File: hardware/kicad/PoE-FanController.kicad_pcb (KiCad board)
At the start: 2 copper layers, 70 x 78 mm, 33 parts, among them J2 FAN1, J3 FAN2, J4 FAN3, J5 FAN4, J6 Molex_KK254_3pin, J8 Waveshare_ESP32P4POEETH, U1 LM2587-12

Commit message: hw(#100): rotate J2-J5 fan headers to horizontal (0deg) and refill zones
Connectors moved to (60, 10/22/34/46) at 0deg rotation so pin row lies
along X-axis (horizontal). GND copper zones refilled to clear new pad
positions. DRC: 0 errors, 16 warnings (baseline unchanged).

Co-authored-by: Copilot <223556219+Copilot@users.noreply.github.com>
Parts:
- moved J2 2.00 mm to (60.0, 10.0), turned to 0 degrees
- moved J3 2.00 mm to (60.0, 22.0), turned to 0 degrees
- moved J4 2.00 mm to (60.0, 34.0), turned to 0 degrees
- moved J5 2.00 mm to (60.0, 46.0), turned to 0 degrees

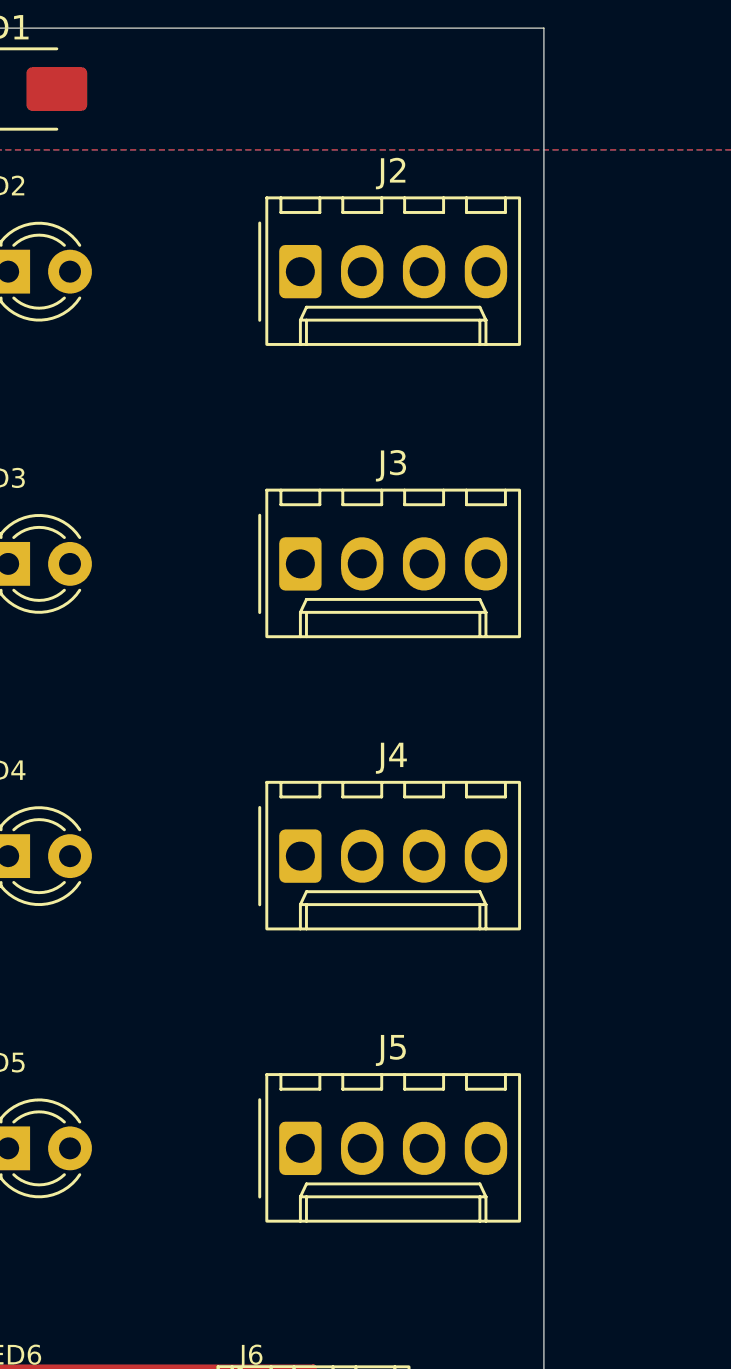
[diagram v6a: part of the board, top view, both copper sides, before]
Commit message: hw(#100): align J2-J5 fan headers to x=58 matching J6 temp-probe connector
All Molex connectors (J2-J6) now share x=58 reference, with pin rows
horizontal (0deg rotation). Zones refilled. DRC: 0 errors, 16 warnings.

Co-authored-by: Copilot <223556219+Copilot@users.noreply.github.com>
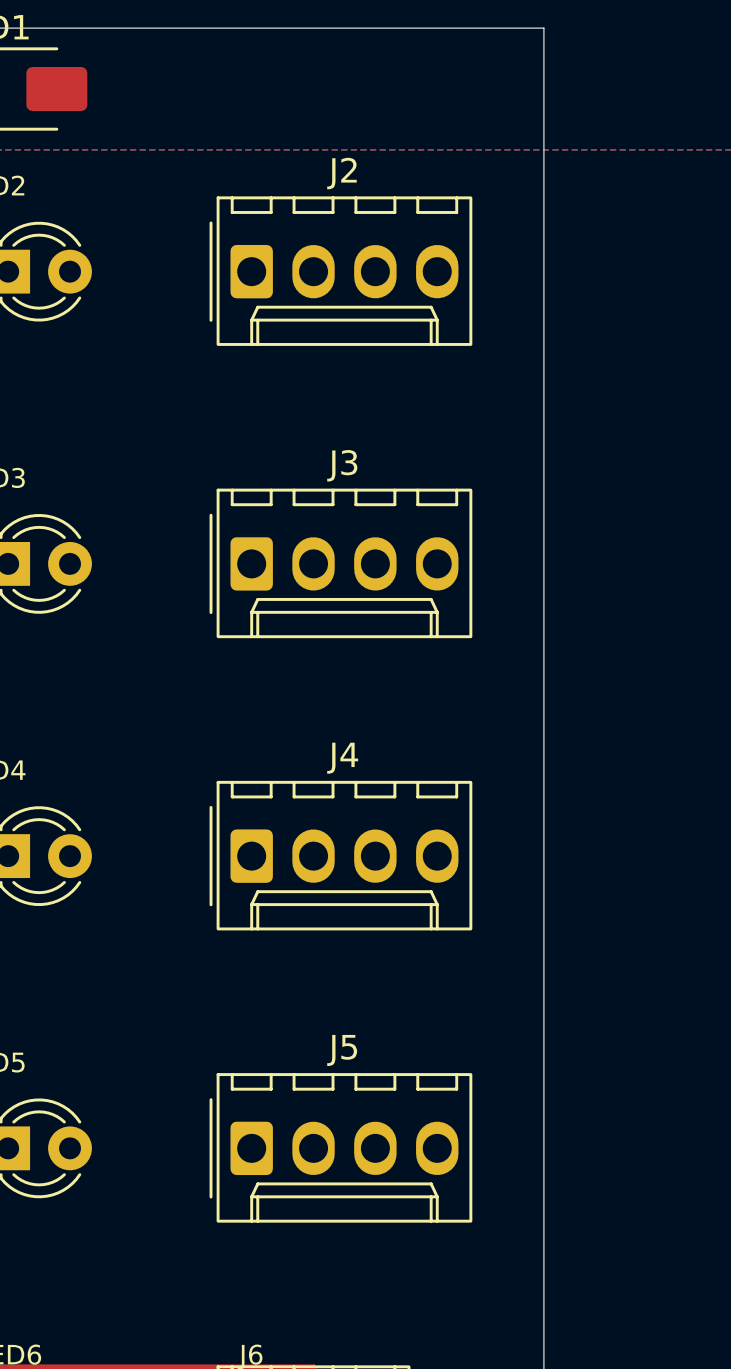
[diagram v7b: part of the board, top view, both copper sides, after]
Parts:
- moved J2 2.00 mm to (58.0, 10.0)
- moved J3 2.00 mm to (58.0, 22.0)
- moved J4 2.00 mm to (58.0, 34.0)
- moved J5 2.00 mm to (58.0, 46.0)
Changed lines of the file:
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@@
 	(footprint "Connector_Molex:Molex_KK-254_AE-6410-04A_1x04_P2.54mm_Vertical"
 		(layer "F.Cu")
-		(at 60 22)
+		(at 58 22)
 		(descr "Molex KK-254 Interconnect System, old/engineering part number: AE-6410-04A example for new part number: 22-27-2041, 4 Pins (http://www.molex.com/pdm_docs/sd/022272021_sd.pdf)")
 		(tags "connector Molex KK-254 vertical")
@@
 	(footprint "Connector_Molex:Molex_KK-254_AE-6410-04A_1x04_P2.54mm_Vertical"
 		(layer "F.Cu")
-		(at 60 46)
+		(at 58 46)
 		(descr "Molex KK-254 Interconnect System, old/engineering part number: AE-6410-04A example for new part number: 22-27-2041, 4 Pins (http://www.molex.com/pdm_docs/sd/022272021_sd.pdf)")
 		(tags "connector Molex KK-254 vertical")
@@
 	(footprint "Connector_Molex:Molex_KK-254_AE-6410-04A_1x04_P2.54mm_Vertical"
 		(layer "F.Cu")
-		(at 60 10)
+		(at 58 10)
 		(descr "Molex KK-254 Interconnect System, old/engineering part number: AE-6410-04A example for new part number: 22-27-2041, 4 Pins (http://www.molex.com/pdm_docs/sd/022272021_sd.pdf)")
 		(tags "connector Molex KK-254 vertical")
@@
 	(footprint "Connector_Molex:Molex_KK-254_AE-6410-04A_1x04_P2.54mm_Vertical"
 		(layer "F.Cu")
-		(at 60 34)
+		(at 58 34)
 		(descr "Molex KK-254 Interconnect System, old/engineering part number: AE-6410-04A example for new part number: 22-27-2041, 4 Pins (http://www.molex.com/pdm_docs/sd/022272021_sd.pdf)")
 		(tags "connector Molex KK-254 vertical")

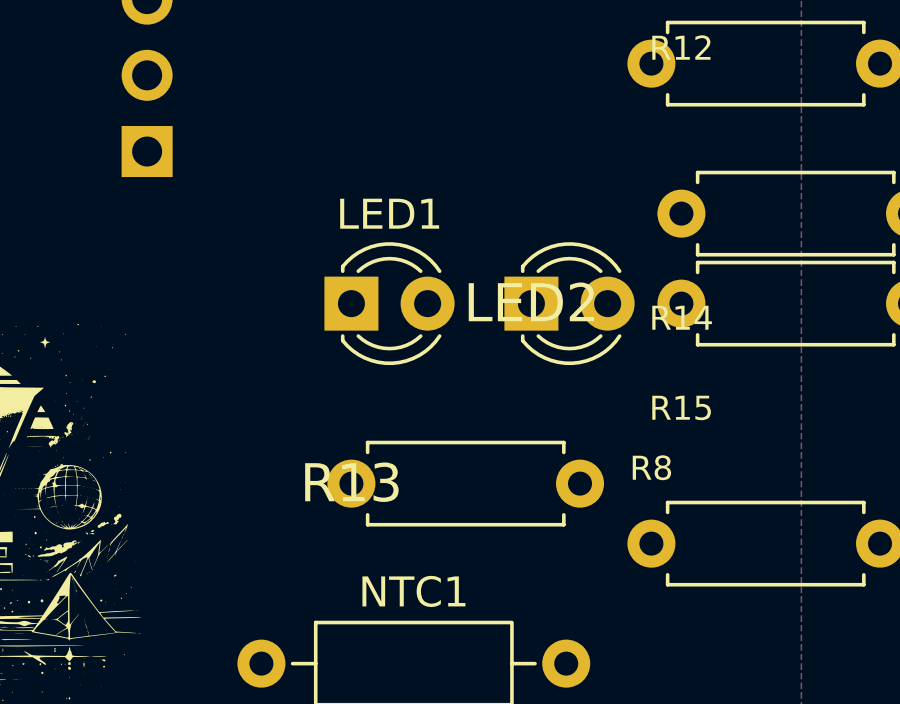
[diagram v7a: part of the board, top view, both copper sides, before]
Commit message: hw(pcb): fix cosmetic PCB issues — R13 dup, LED text, 3D model, User.Comments
- Hide duplicate R13 silkscreen reference (F.Fab label still visible)
- Shrink LED1/LED2 reference text to 0.6mm, hide value labels to
  eliminate LED_GREEN/LED_ORANGE silkscreen overlap
- Add missing 3D model to LED2 (LED_THT:LED_D3.0mm.step)
- Remove 3 User.Comments texts: 'PoE Primary Side', 'SELV Secondary Side',
  'KEEP >= 3mm clearance across dashed line!'
- GND zone (x=40-70) retained: intentional PoE secondary-side GND pour
DRC: 0 errors, 16 warnings (baseline unchanged)

Co-authored-by: Copilot <223556219+Copilot@users.noreply.github.com>
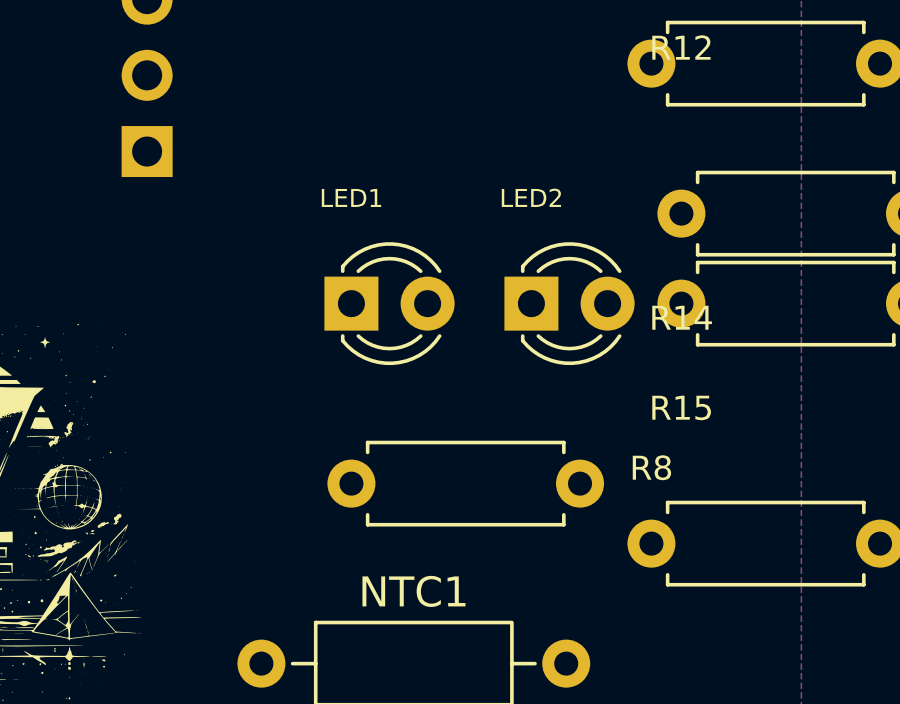
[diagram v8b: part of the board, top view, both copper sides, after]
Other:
- board text removed: "KEEP >= 3mm clearance across dashed line!"
- board text removed: "PoE Primary Side"
- board text removed: "SELV Secondary Side"
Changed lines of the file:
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@@
 		(tags "LED")
 		(property "Reference" "LED1"
-			(at 1.27 -2.96 0)
+			(at 0 -3.5 0)
 			(layer "F.SilkS")
 			(effects
 				(font
-					(size 1 1)
+					(size 0.6 0.6)
 					(thickness 0.15)
 				)
@@
 			(at 1.27 2.96 0)
 			(layer "F.Fab")
+			(hide yes)
 			(effects
 				(font
@@
 		(at 31 58)
 		(property "Reference" "LED2"
-			(at 0 0 0)
+			(at 0 -3.5 0)
 			(layer "F.SilkS")
 			(effects
 				(font
-					(size 1.27 1.27)
+					(size 0.6 0.6)
 				)
 			)
@@
 			(at 0 0 0)
 			(layer "F.Fab")
+			(hide yes)
 			(effects
 				(font
@@
 		)
 		(embedded_fonts no)
+		(model "${KICAD10_3DMODEL_DIR}/LED_THT.3dshapes/LED_D3.0mm.step"
+			(offset
+				(xyz 0 0 0)
+			)
+			(scale
+				(xyz 1 1 1)
+			)
+			(rotate
+				(xyz 0 0 0)
+			)
+		)
 	)
 	(footprint "R_Axial_DIN0207_L6.3mm_D2.5mm_P7.62mm_Horizontal"
@@
 			(at 0 0 0)
 			(layer "F.SilkS")
+			(hide yes)
 			(effects
 				(font
@@
 			)
 		)
-	)
-	(gr_text "PoE Primary Side"
-		(at 20 8 0)
-		(layer "Cmts.User")
-		(effects
-			(font
-				(size 1 1)
-				(thickness 0.1)
-			)
-		)
-	)
-	(gr_text "SELV Secondary Side"
-		(at 21 8 0)
-		(layer "Cmts.User")
-		(effects
-			(font
-				(size 1 1)
-				(thickness 0.1)
-			)
-		)
-	)
-	(gr_text "KEEP >= 3mm clearance across dashed line!"
-		(at 21 11 0)
-		(layer "Cmts.User")
-		(effects
-			(font
-				(size 1.2 1.2)
-				(thickness 0.12)
-			)
-		)
